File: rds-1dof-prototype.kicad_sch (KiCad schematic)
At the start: 10 parts, among them U1 Teensy4.0

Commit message: Formatting updates
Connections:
- new net: M2006P1. (in_c), Odrive_pro1. (DC-) (x2)
- new net: AS5048. (+5V), Odrive_pro1. (DC-) (x4)
- new net: E-stop1. (+V_OUT), LRS-1. (GND)
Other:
- note added: "Encoder"
- note added: "MCU"
- note added: "Motor"
- note added: "Odrive"
- note added: "Power"
- note added: "Transmitter"
- company: (none) -> RDS Speedster Team 2026
- title: (none) -> RDS 1-DOF Prototype
- moved on the sheet: AS5048, C3, C4, E-stop1, LRS-1, M2006P1, MCP2562, R4, U1

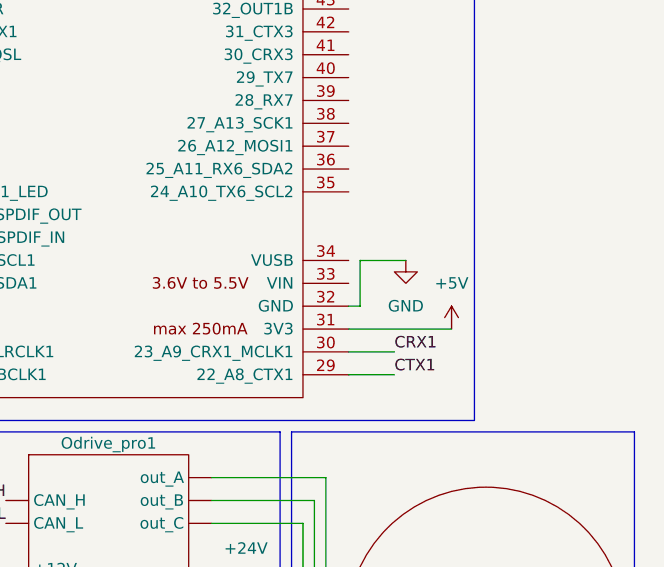
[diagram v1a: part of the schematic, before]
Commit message: added 3.3V power from teensy
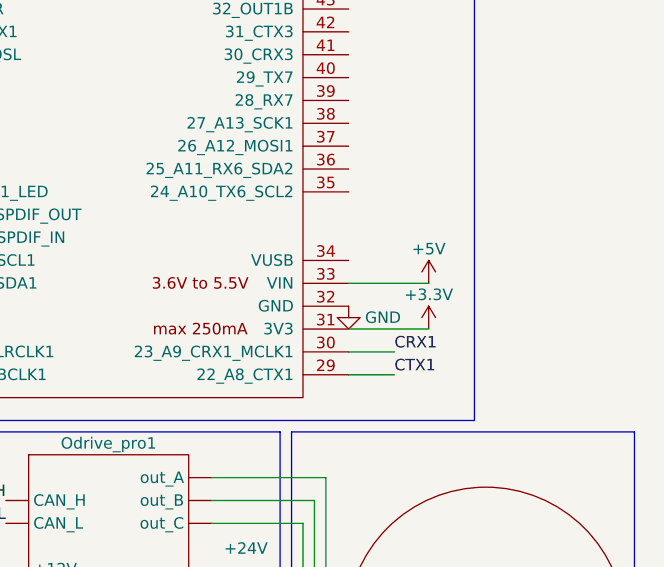
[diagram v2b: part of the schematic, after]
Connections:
- net +3.3V: now also U1.31 (3V3)
- net +5V: now also U1.33 (VIN); no longer U1.31 (3V3)
- new net: M2006P1. (in_c), Odrive_pro1. (DC-) (x2)
- new net: AS5048. (+5V), Odrive_pro1. (DC-) (x4)
- new net: E-stop1. (+V_OUT), LRS-1. (GND)
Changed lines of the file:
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@@
 	(wire
 		(pts
-			(xy 104.14 102.87) (xy 104.14 107.95)
+			(xy 111.76 105.41) (xy 102.87 105.41)
 		)
 		(stroke
@@
 	(wire
 		(pts
-			(xy 114.3 110.49) (xy 102.87 110.49)
+			(xy 111.76 110.49) (xy 102.87 110.49)
 		)
 		(stroke
@@
 	(wire
 		(pts
-			(xy 104.14 107.95) (xy 102.87 107.95)
-		)
-		(stroke
-			(width 0)
-			(type default)
-		)
-	)
-	(wire
-		(pts
 			(xy 62.23 137.16) (xy 64.77 137.16)
 		)
@@
 		(pts
 			(xy 80.01 31.75) (xy 82.55 31.75)
-		)
-		(stroke
-			(width 0)
-			(type default)
-		)
-	)
-	(wire
-		(pts
-			(xy 109.22 102.87) (xy 104.14 102.87)
 		)
 		(stroke
@@
 	(symbol
 		(lib_id "power:GND")
-		(at 109.22 102.87 0)
+		(at 102.87 107.95 0)
 		(unit 1)
 		(exclude_from_sim no)
@@
 		(dnp no)
 		(property "Reference" "#PWR026"
-			(at 109.22 109.22 0)
+			(at 102.87 114.3 0)
 			(effects
 				(font
@@
 		)
 		(property "Value" "GND"
-			(at 109.22 107.95 0)
+			(at 106.68 109.22 0)
 			(effects
 				(font
@@
 		)
 		(property "Footprint" ""
-			(at 109.22 102.87 0)
+			(at 102.87 107.95 0)
 			(effects
 				(font
@@
 		)
 		(property "Datasheet" ""
-			(at 109.22 102.87 0)
+			(at 102.87 107.95 0)
 			(effects
 				(font
@@
 		)
 		(property "Description" "Power symbol creates a global label with name \"GND\" , ground"
-			(at 109.22 102.87 0)
+			(at 102.87 107.95 0)
 			(effects
 				(font
@@
 	(symbol
 		(lib_id "power:+5V")
-		(at 114.3 110.49 0)
+		(at 111.76 105.41 0)
 		(unit 1)
 		(exclude_from_sim no)
@@
 		(on_board yes)
 		(dnp no)
-		(fields_autoplaced yes)
 		(property "Reference" "#PWR05"
-			(at 114.3 114.3 0)
+			(at 111.76 109.22 0)
 			(effects
 				(font
@@
 		)
 		(property "Value" "+5V"
-			(at 114.3 105.41 0)
+			(at 111.76 101.6 0)
 			(effects
 				(font
@@
 		)
 		(property "Footprint" ""
-			(at 114.3 110.49 0)
+			(at 111.76 105.41 0)
 			(effects
 				(font
@@
 		)
 		(property "Datasheet" ""
-			(at 114.3 110.49 0)
+			(at 111.76 105.41 0)
 			(effects
 				(font
@@
 		)
 		(property "Description" "Power symbol creates a global label with name \"+5V\""
-			(at 114.3 110.49 0)
+			(at 111.76 105.41 0)
 			(effects
 				(font
@@
 					(unit 1)
 				)
+			)
+		)
+	)
+	(symbol
+		(lib_id "power:+3.3V")
+		(at 111.76 110.49 0)
+		(unit 1)
+		(exclude_from_sim no)
+		(in_bom yes)
+		(on_board yes)
+		(dnp no)
+		(property "Reference" "#PWR06"
+			(at 111.76 114.3 0)
+			(effects
+				(font
+					(size 1.27 1.27)
+				)
+				(hide yes)
+			)
+		)
+		(property "Value" "+3.3V"
+			(at 111.76 106.68 0)
+			(effects
+				(font
+					(size 1.27 1.27)
+				)
+			)
+		)
+		(property "Footprint" ""
+			(at 111.76 110.49 0)
+			(effects
+				(font
+					(size 1.27 1.27)
+				)
+				(hide yes)
+			)
+		)
+		(property "Datasheet" ""
+			(at 111.76 110.49 0)
+			(effects
+				(font
+					(size 1.27 1.27)
+				)
+				(hide yes)
+			)
+		)
+		(property "Description" "Power symbol creates a global label with name \"+3.3V\""
+			(at 111.76 110.49 0)
+			(effects
+				(font
+					(size 1.27 1.27)
+				)
+				(hide yes)
+			)
+		)
+		(pin "1"
+		)
+		(instances
+			(project ""
+				(path "/3f513f6b-8cac-4078-9835-772e37441c61"
+					(reference "#PWR06")
+					(unit 1)
+				)

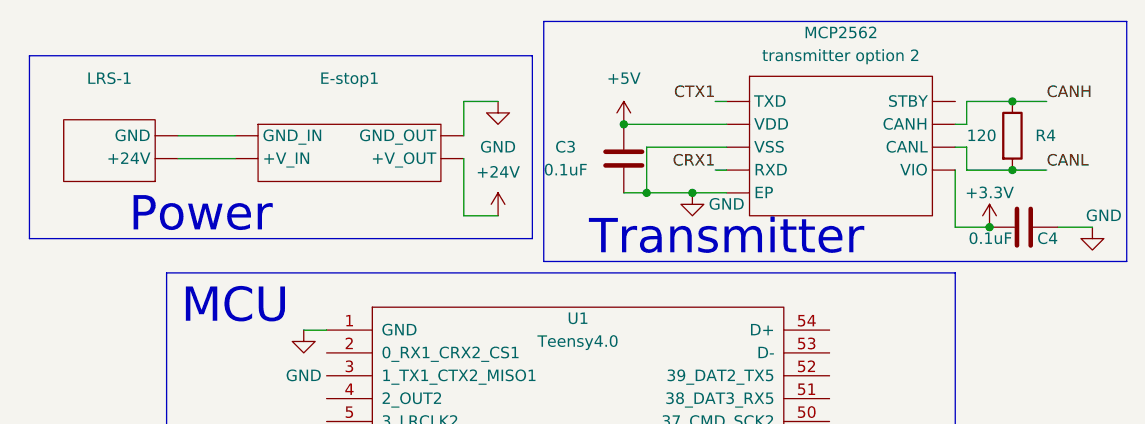
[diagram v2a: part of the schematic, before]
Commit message: edited brake resistor circuit
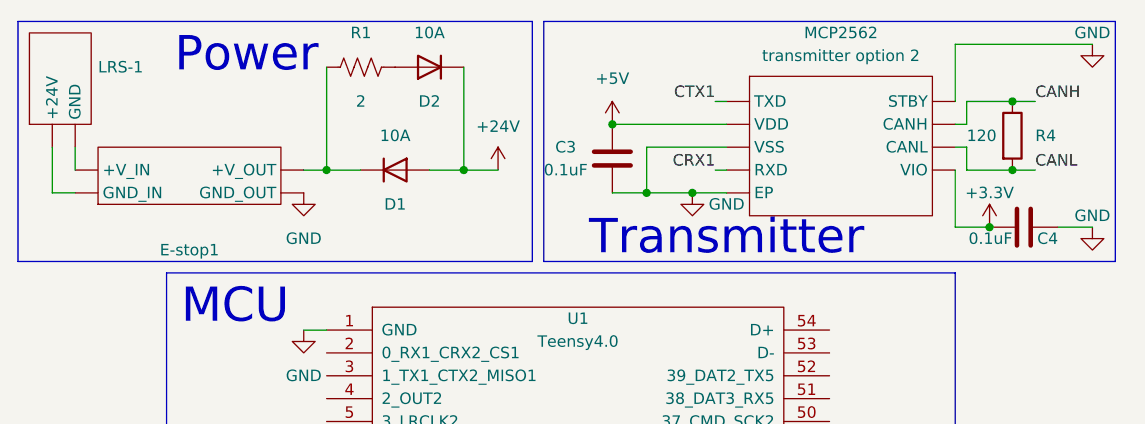
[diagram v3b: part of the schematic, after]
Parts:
- added D1, D2: 10A, symbol Diode:1N4148WT
- added R1: 2, symbol Device:R_US
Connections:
- net +24V: now also D1.2 (A), D2.1 (K); no longer E-stop1. (+V_OUT)
- new net: M2006P1. (in_c), Odrive_pro1. (DC-) (x2)
- new net: D2.2 (A), R1.2
- new net: AS5048. (+5V), Odrive_pro1. (DC-) (x4)
- new net: D1.1 (K), E-stop1. (+V_OUT), R1.1
- new net: E-stop1. (+V_OUT), LRS-1. (GND)
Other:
- moved on the sheet: C3, E-stop1, LRS-1

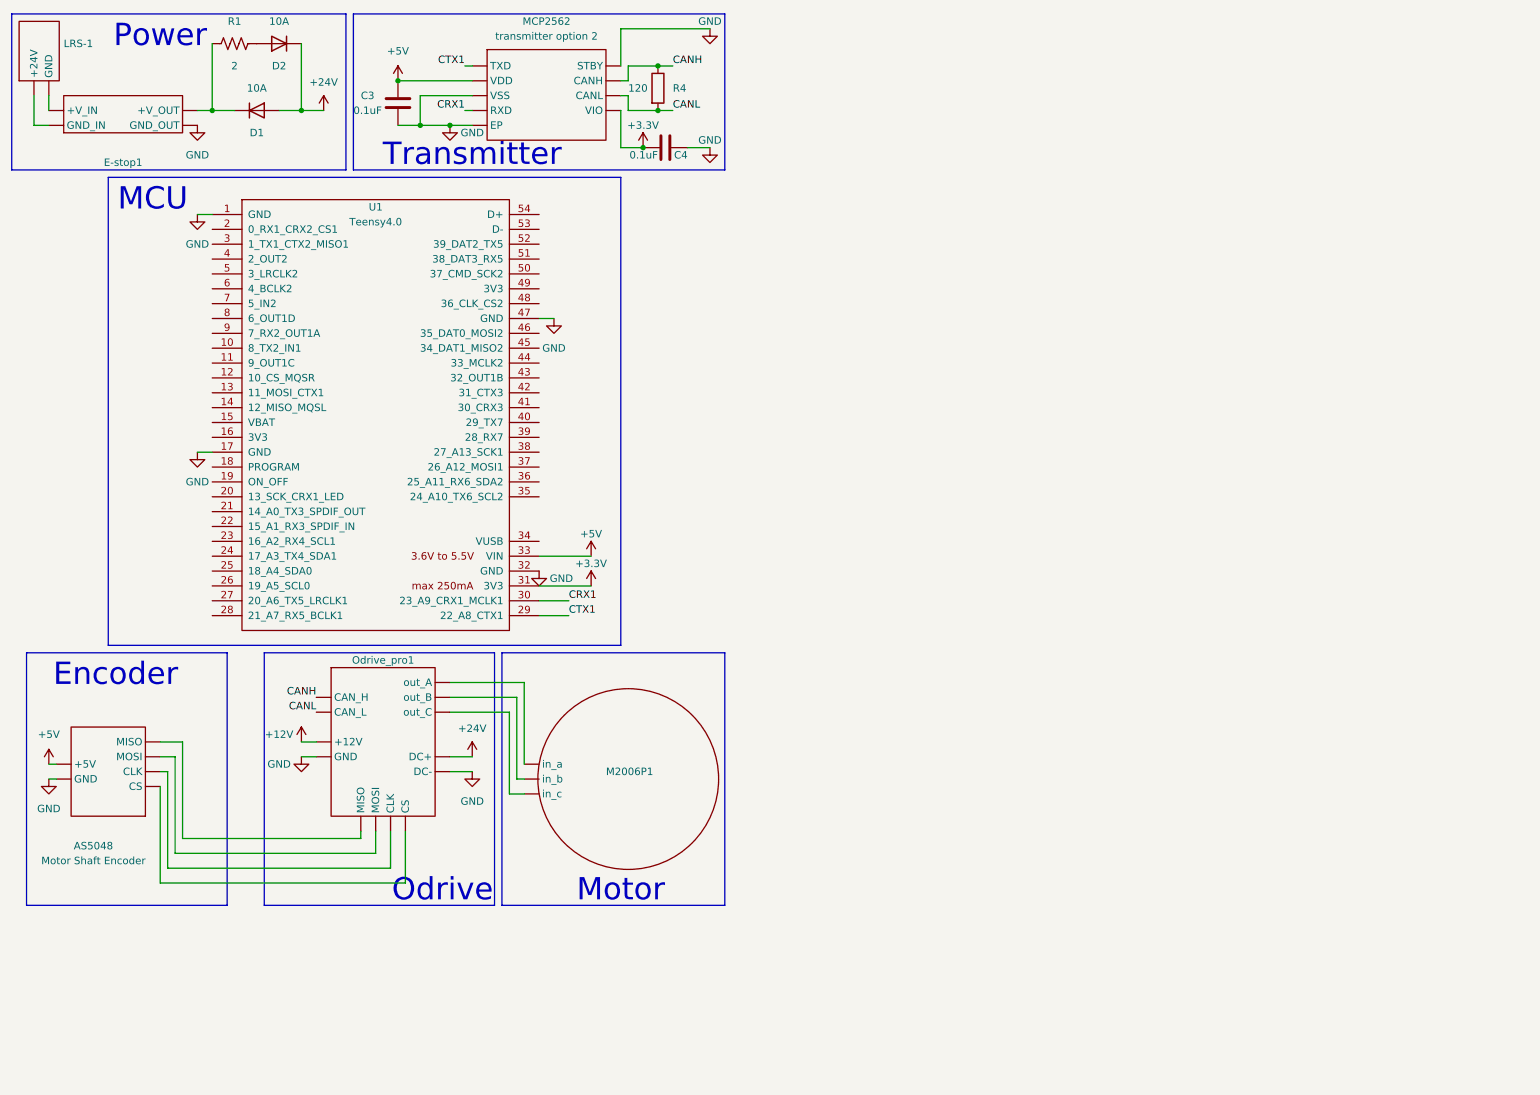
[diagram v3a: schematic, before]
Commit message: updated for 3 motors
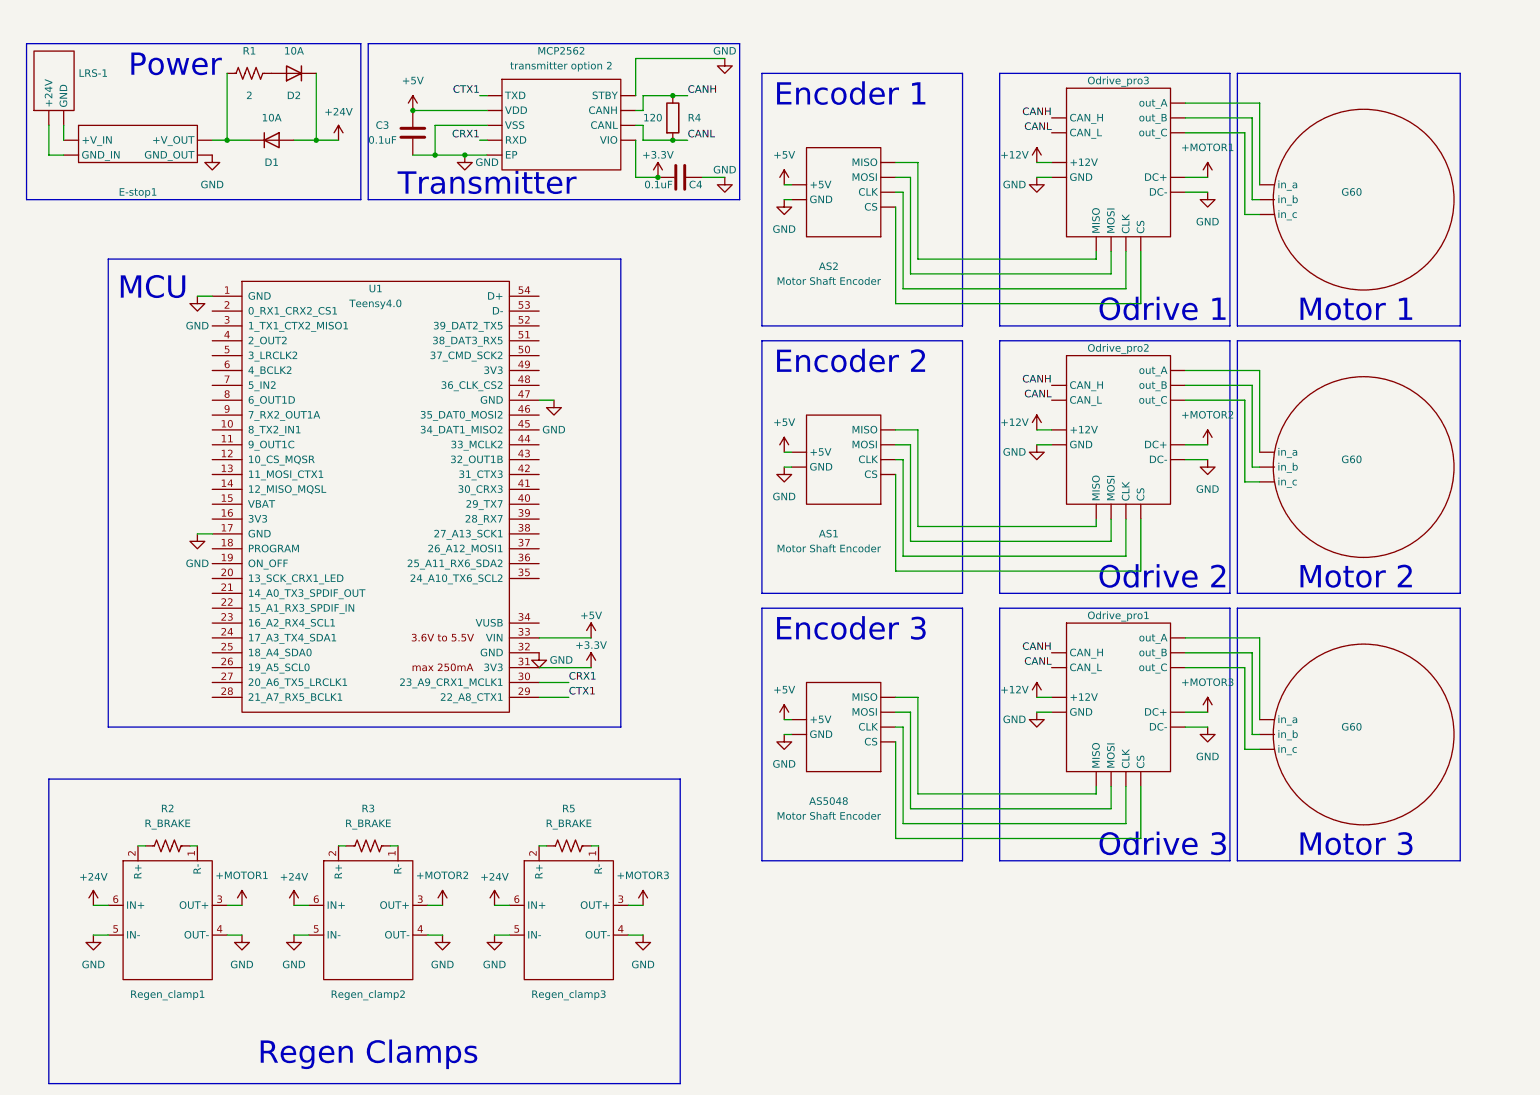
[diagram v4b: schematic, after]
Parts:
- added AS1, AS2: Motor Shaft Encoder, symbol RDS_lib:AMT223C-V
- added G60 (x2): ~, symbol RDS_lib:M2006 P36
- added Odrive_pro2, Odrive_pro3: ~, symbol RDS_lib:odrive_pro
- added R2, R3, R5: R_BRAKE, symbol Device:R_US
- added Regen_clamp1, Regen_clamp2, Regen_clamp3: ~, symbol RDS_lib:regen_clamp
- renumbered M2006P1 to G60
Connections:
- net +12V: now also Odrive_pro2. (DC-), Odrive_pro3. (DC-)
- net +24V: now also Regen_clamp1.6 (IN+), Regen_clamp2.6 (IN+), Regen_clamp3.6 (IN+); no longer Odrive_pro1. (DC-)
- net +5V: now also AS1. (+5V), AS2. (+5V)
- net CANH: now also Odrive_pro2. (DC-), Odrive_pro3. (DC-)
- net CANL: now also Odrive_pro2. (DC-), Odrive_pro3. (DC-)
- net GND: now also AS1. (+5V), AS2. (+5V), Odrive_pro2. (DC-), Odrive_pro3. (DC-), Regen_clamp1.4 (OUT-), Regen_clamp1.5 (IN-), Regen_clamp2.4 (OUT-), Regen_clamp2.5 (IN-), Regen_clamp3.4 (OUT-), Regen_clamp3.5 (IN-)
- new net: G60. (in_c), Odrive_pro2. (DC-) (x3)
- new net: AS1. (+5V), Odrive_pro2. (DC-) (x4)
- new net: R5.1, Regen_clamp3.2 (R+)
- new net: R5.2, Regen_clamp3.1 (R-)
- new net: G60. (in_c), Odrive_pro3. (DC-) (x3)
- new net: R3.2, Regen_clamp2.1 (R-)
- new net: R3.1, Regen_clamp2.2 (R+)
- new net: G60. (in_c), Odrive_pro1. (DC-) (x2)
- new net: AS5048. (+5V), Odrive_pro1. (DC-) (x4)
- new net: E-stop1. (+V_OUT), LRS-1. (GND)
- new net: AS2. (+5V), Odrive_pro3. (DC-) (x4)
- new net: R2.2, Regen_clamp1.1 (R-)
- new net: R2.1, Regen_clamp1.2 (R+)
- new net +MOTOR1: Odrive_pro3. (DC-), Regen_clamp1.3 (OUT+)
- new net +MOTOR2: Odrive_pro2. (DC-), Regen_clamp2.3 (OUT+)
- new net +MOTOR3: Odrive_pro1. (DC-), Regen_clamp3.3 (OUT+)
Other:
- note added: "Encoder 1"
- note added: "Encoder 2"
- note added: "Encoder 3"
- note added: "Motor 1"
- note added: "Motor 2"
- note added: "Motor 3"
- note added: "Odrive 1"
- note added: "Odrive 2"
- note added: "Odrive 3"
- note added: "Regen Clamps"
- note removed: "Encoder"
- note removed: "Motor"
- note removed: "Odrive"
- moved on the sheet: AS5048, C3, C4, D1, D2, E-stop1, G60, LRS-1, MCP2562, Odrive_pro1, R1, R4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
